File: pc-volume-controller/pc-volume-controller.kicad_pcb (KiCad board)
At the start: 2 copper layers, 120 x 85 mm, 16 parts, among them U1 Arduino_Nano_v3.x

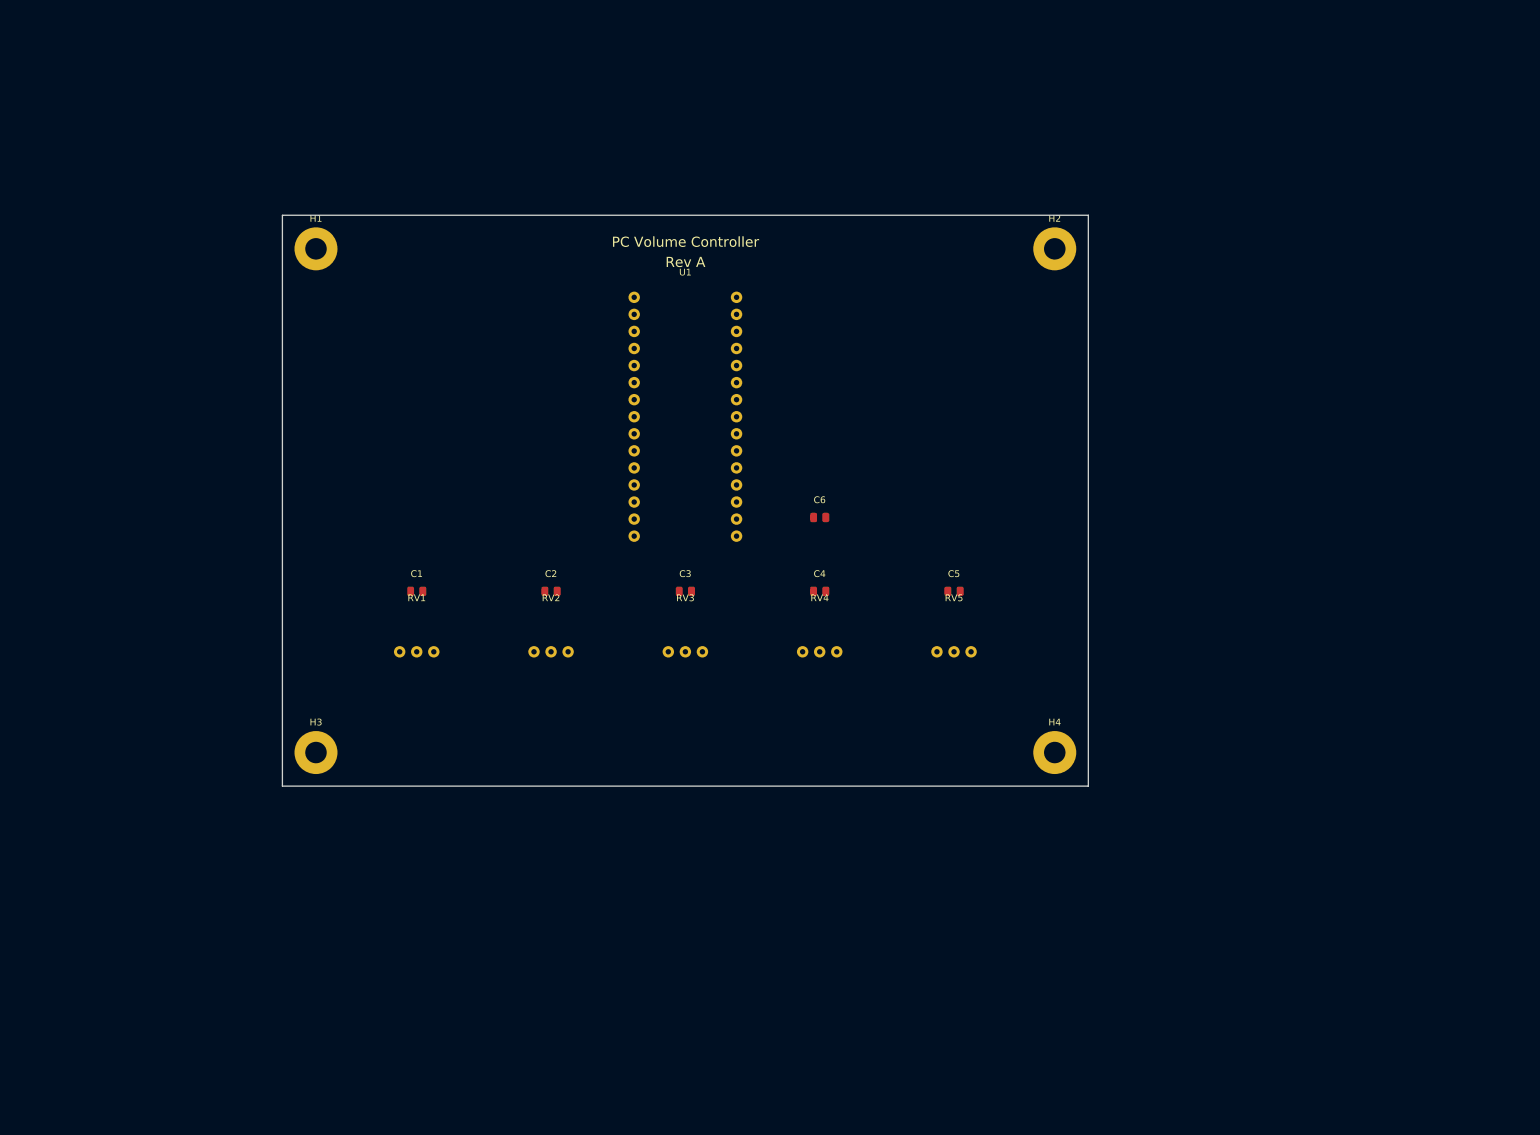
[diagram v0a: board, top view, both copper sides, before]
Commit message: Rebuild with real KiCad 9 libraries; verified by kicad-cli ERC/DRC
KiCad is now installed on this host, so the generated project was validated
against KiCad itself rather than only the kicad-happy Python tooling. That
validation found real defects in what had been delivered:

pc-volume-controller.kicad_sch
* now embeds the actual MCU_Module:Arduino_Nano_v3.x, Device:R_Potentiometer,
  Device:C, power:* and Mechanical:MountingHole definitions instead of
  hand-authored symbols (fixes 37 lib_symbol_mismatch warnings)
* every coordinate snapped to the 1.27 mm grid (fixes 70 endpoint_off_grid)
* real library footprints assigned, replacing the invented 'pvc:' namespace
* ERC: 125 violations -> 0

The Nano pinout is now verified rather than assumed: the official symbol
confirms A0-A4 = pins 19-23, +5V = pin 27, GND = pins 4 and 29.

pc-volume-controller.kicad_pcb
* rebuilt from the real Module:Arduino_Nano, Potentiometer_THT and
  Capacitor_SMD footprints with all pads netted
* board fully routed on 2 layers (B.Cu horizontals, F.Cu verticals)
* DRC: 89 violations -> 0, with 0 unconnected items and 0 schematic-parity
  differences

LED/LED-revised.kicad_sch
* added the PWR_FLAG the GND net needs (the battery's negative pin is passive,
  so ERC reported power_pin_not_driven)
* ERC: 1 error -> 0

Validation notes: kicad-cli 9.0.2. Notable format findings - a .kicad_pcb may
not carry a top-level (uuid ...) node (KiCad refuses the board), gr_line stroke
type must be the bare atom 'solid' not a quoted string, and an embedded symbol
must keep leading atoms on its opening line.
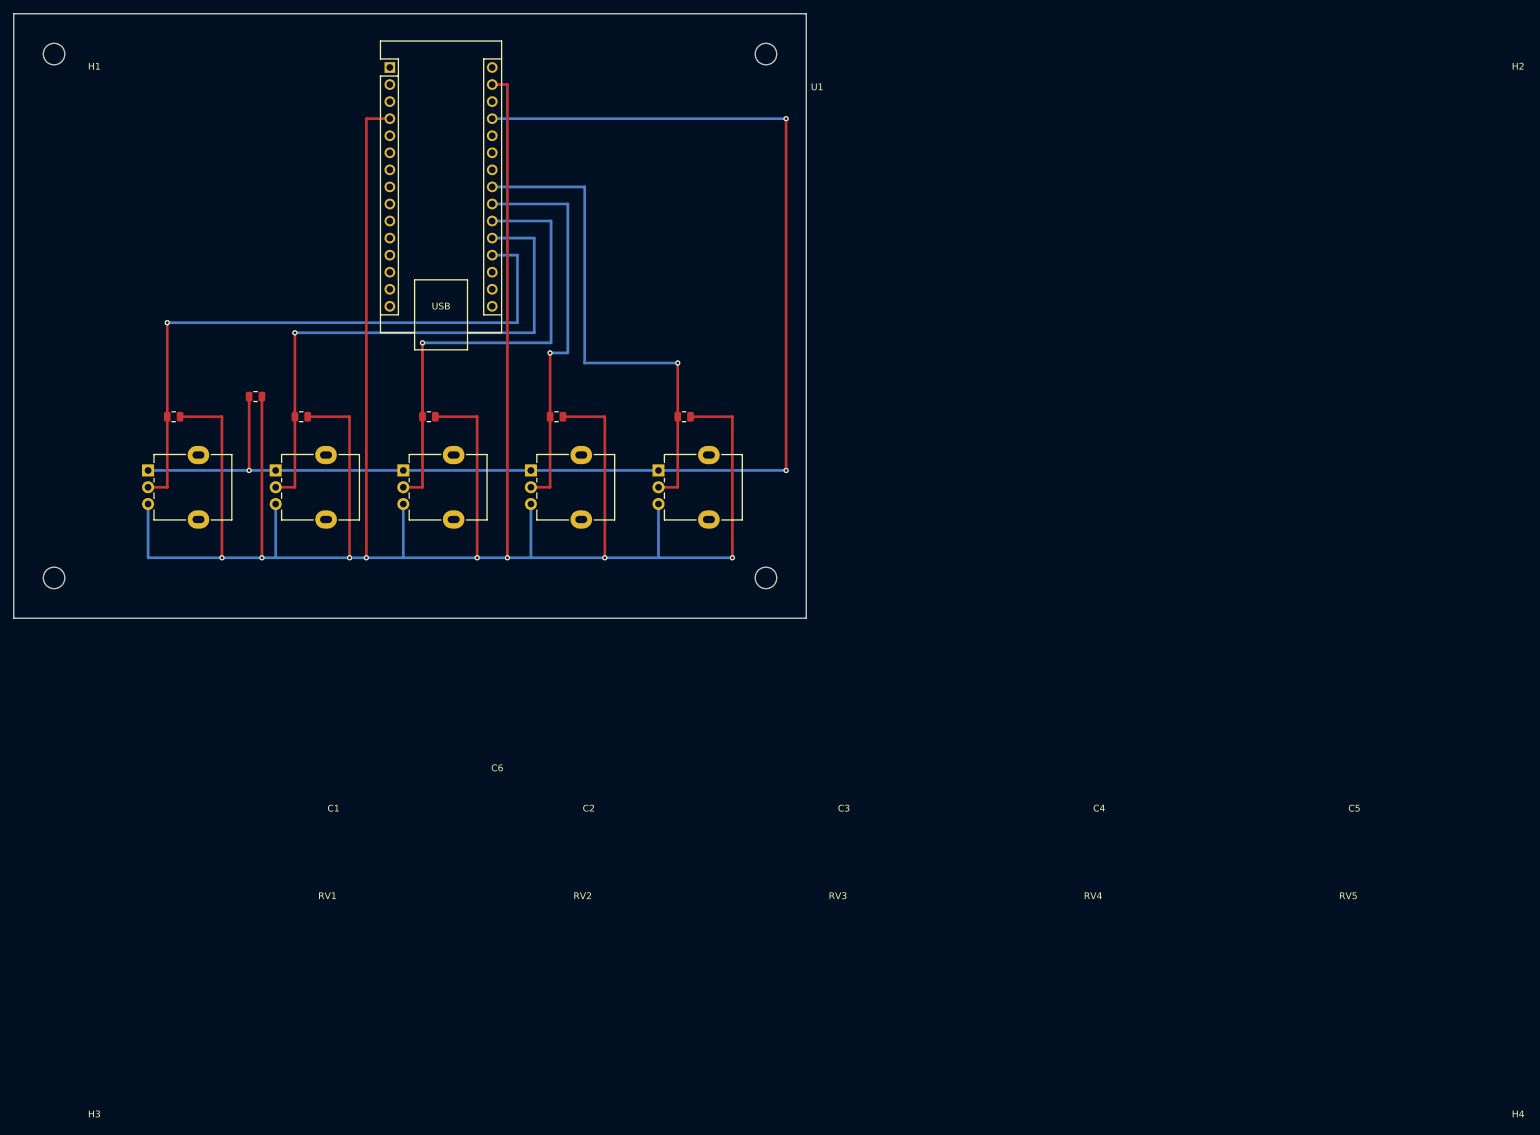
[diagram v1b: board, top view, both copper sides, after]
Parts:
- C1, C2, C3, C4, C5, C6: footprint pvc:C_0805_2012Metric -> Capacitor_SMD:C_0805_2012Metric
- H1, H2, H3, H4: footprint pvc:MountingHole_M3 -> MountingHole:MountingHole_3.2mm_M3
- RV1, RV2, RV3, RV4, RV5: footprint pvc:Potentiometer_9mm_PanelMount_THT -> Potentiometer_THT:Potentiometer_Alpha_RD901F-40-00D_Single_Vertical
- U1: footprint pvc:Arduino_Nano_30pin_THT -> Module:Arduino_Nano
- moved C6 85.9 mm to (36.0, 57.0)
- moved U1 68.1 mm to (56.0, 8.00)
- moved H2 51.9 mm to (112.0, 6.00)
- moved RV5 51.6 mm to (96.0, 68.0)
- moved RV4 50.8 mm to (77.0, 68.0)
- moved H4 50.2 mm to (112.0, 84.0)
- moved RV3 49.9 mm to (58.0, 68.0)
- moved RV2 49.1 mm to (39.0, 68.0)
- moved H1 48.6 mm to (6.00, 6.00)
- moved RV1 48.3 mm to (20.0, 68.0)
- moved C5 47.9 mm to (99.8, 60.0)
- moved C4 47.0 mm to (80.8, 60.0)
- moved H3 46.9 mm to (6.00, 84.0)
- moved C3 46.2 mm to (61.8, 60.0)
- moved C2 45.4 mm to (42.8, 60.0)
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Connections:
- net VOL1 renamed /VOL1
- net VOL2 renamed /VOL2
- net VOL3 renamed /VOL3
- net VOL4 renamed /VOL4
- net VOL5 renamed /VOL5
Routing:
- net GND: track 0.00 -> 428.8 mm, vias 0 -> 8
- net +5V: track 0.00 -> 202.1 mm, vias 0 -> 3
- net /VOL1: track 0.00 -> 93.3 mm, vias 0 -> 1
- net /VOL2: track 0.00 -> 81.9 mm, vias 0 -> 1
- net /VOL5: track 0.00 -> 75.2 mm, vias 0 -> 1
- net /VOL3: track 0.00 -> 70.4 mm, vias 0 -> 1
- net /VOL4: track 0.00 -> 58.9 mm, vias 0 -> 1
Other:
- board size 120 x 85 mm -> 118 x 90 mm
- board text removed: "PC Volume Controller"
- board text removed: "Rev A"

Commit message: Compact rectangular PCB: 118x90 -> 98x54 mm, functional pot row
Addresses the layout feedback: compress the board toward a rectangle and put the
potentiometers on a usable panel pitch.

What changed (PCB only - the circuit and schematic are untouched, netlist
verified identical):

* Board 118 x 90 mm -> 98 x 54 mm, a 1.81:1 rectangle and 50% less area.
* Five pots now sit in one evenly spaced row along the top edge at 17.78 mm
  (0.700 in) pitch - a standard panel pitch - so the knob shafts line up on a
  single panel line. The real footprint's courtyard is 13.75 mm wide, so this
  leaves ~4 mm between neighbours for the knob and for hand wiring.
* The Arduino Nano is rotated 90 deg. Un-rotated, its 46 mm length forces either
  a very tall board or puts the USB connector under the pot row; rotated, the
  board is half the height AND the USB exits the left board edge.
* Pot X positions land on GAP CENTRES of the Nano's 2.54 mm pad grid, so wiper
  signals dive BETWEEN the Nano's pins instead of being routed around the
  module. Each wiper steps 2.54 mm sideways first, because pot pin 3 shares its
  X with the wiper.
* /VOLn channel ordering chosen so no channel is crossed by another net's
  descent: VOL1..VOL5 at y = 30/28/32/34/36.
* C6 moved from the far right (about 80 mm from the Nano supply pins) to the
  left edge beside them.

KiCad 9 format details re-learned the hard way while doing this (both were
silently wrong in earlier revisions):
* A footprint property's (at ...) in a .kicad_pcb is RELATIVE to the footprint
  origin, not absolute.
* For a ROTATED footprint that offset is rotated too, so an absolute target must
  be de-rotated into the footprint's local frame before storing.
* A footprint's pad UUIDs come from the library; embedding one footprint several
  times duplicates them and KiCad then blames the wrong reference. They must be
  regenerated per placement.
* The Nano footprint's 90 deg rotation makes KiCad report a
  lib_footprint_mismatch warning 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
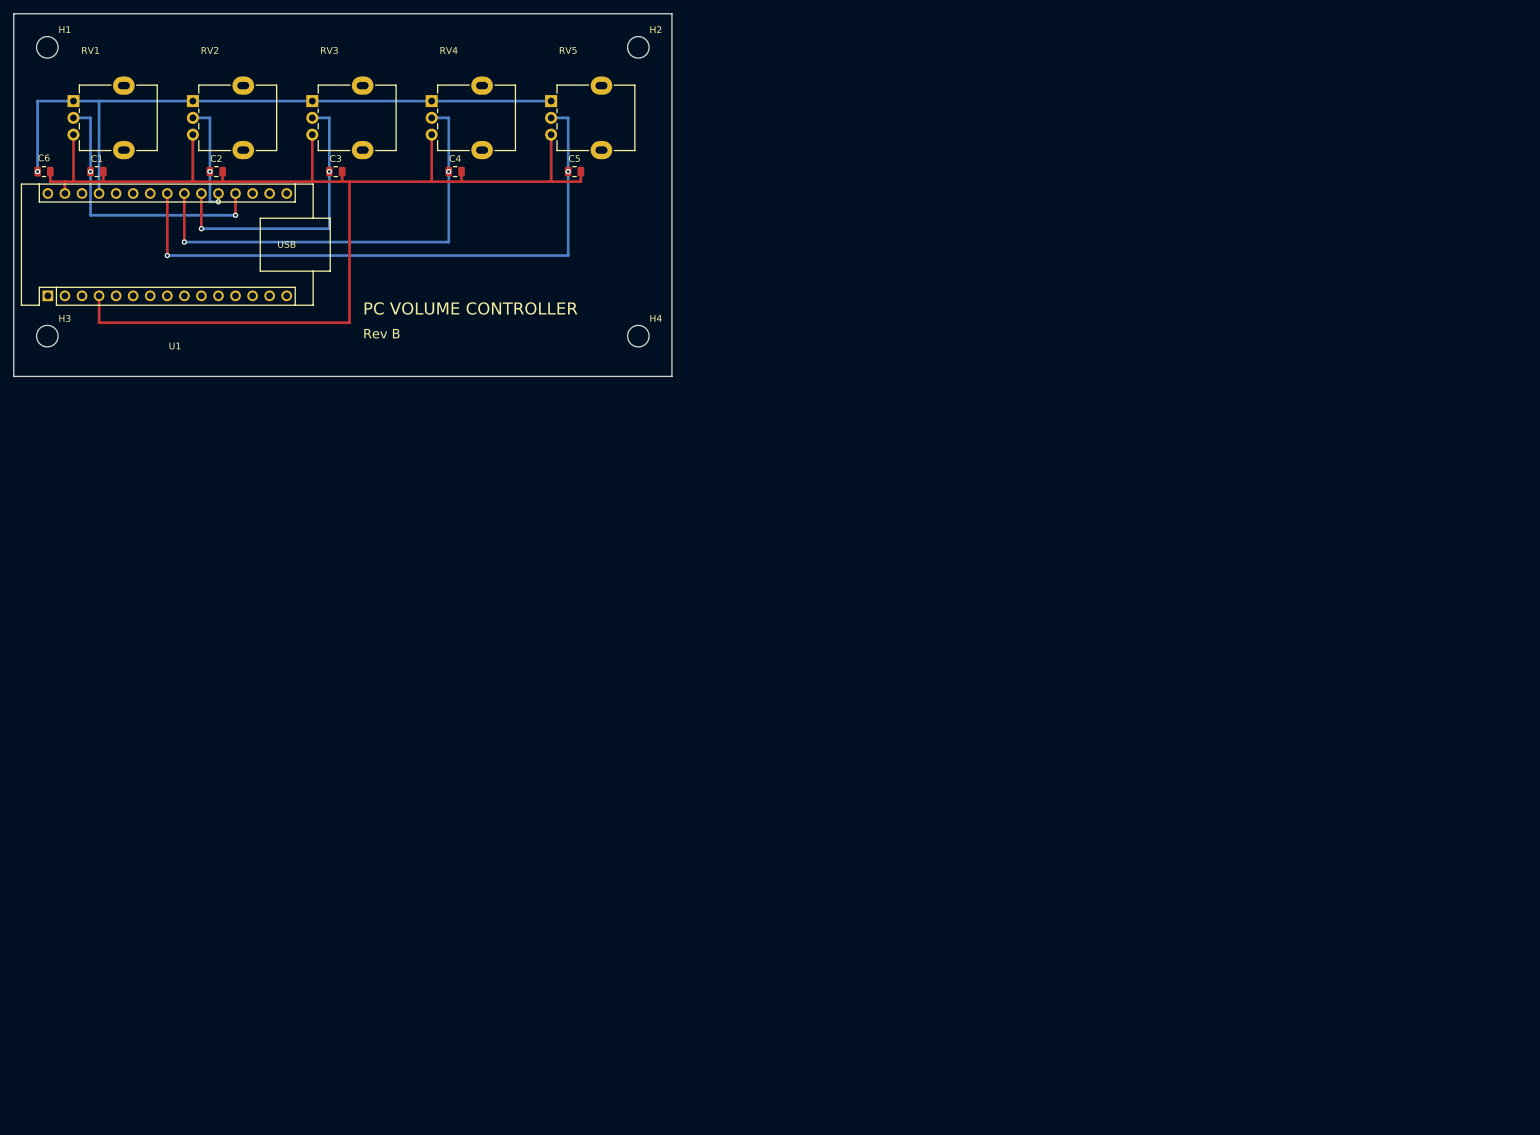
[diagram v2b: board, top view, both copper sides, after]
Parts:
- moved U1 61.2 mm to (5.08, 42.0), turned to 90 degrees
- moved RV5 57.3 mm to (80.0, 13.0)
- moved RV4 56.9 mm to (62.2, 13.0)
- moved RV3 56.6 mm to (44.5, 13.0)
- moved RV2 56.4 mm to (26.7, 13.0)
- moved RV1 56.1 mm to (8.89, 13.0)
- moved C6 46.0 mm to (4.50, 23.5)
- moved H4 40.7 mm to (93.0, 48.0)
- moved C5 40.0 mm to (83.5, 23.5)
- moved C4 39.5 mm to (65.7, 23.5)
- moved C3 39.0 mm to (47.9, 23.5)
- moved C2 38.6 mm to (30.2, 23.5)
- moved C1 38.2 mm to (12.4, 23.5)
- moved H3 36.0 mm to (5.00, 48.0)
- moved H2 19.0 mm to (93.0, 5.00)
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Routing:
- net GND: track 428.8 -> 187.1 mm, vias 8 -> 0
- net +5V: track 202.1 -> 100.7 mm, vias 3 -> 1
- net /VOL2: track 81.9 -> 17.5 mm, vias 1 -> 2
- net /VOL1: track 93.3 -> 41.9 mm, vias 1 -> 2
- net /VOL3: track 70.4 -> 43.3 mm, vias 1 -> 2
- net /VOL5: track 75.2 -> 92.0 mm, vias 1 -> 2
- net /VOL4: track 58.9 -> 67.6 mm, vias 1 -> 2
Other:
- board size 118 x 90 mm -> 98 x 54 mm
- board text added: "PC VOLUME CONTROLLER"
- board text added: "Rev B"
